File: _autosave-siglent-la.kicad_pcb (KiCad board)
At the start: 4 copper layers, 21.6 x 32.8 mm, 65 parts, among them J1 Bus_PCI_Express_x1, J10 IPEX-004, J12 IPEX-004, J13 IPEX-004, J14 IPEX-004, J15 IPEX-004, J16 IPEX-004, J17 IPEX-004, J18 IPEX-004, J19 IPEX-004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

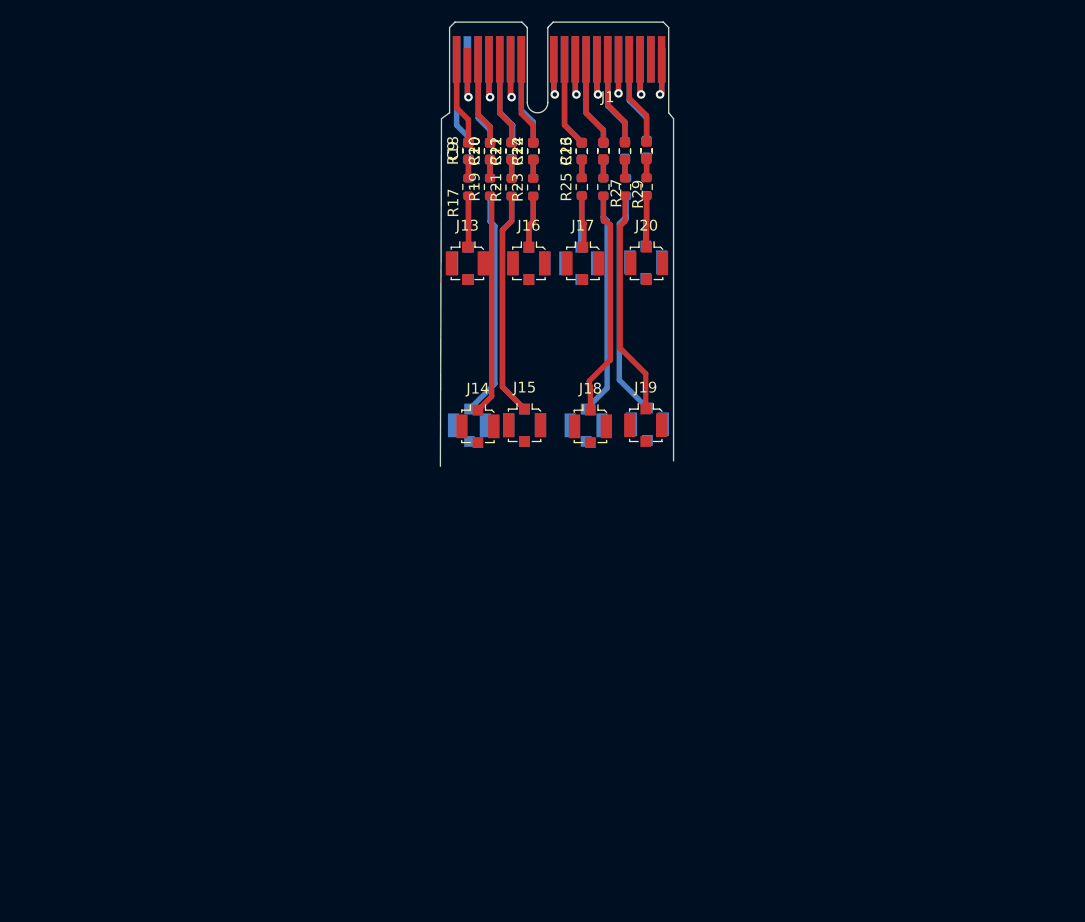
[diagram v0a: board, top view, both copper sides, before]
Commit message: rj45 version of the logic analyzer
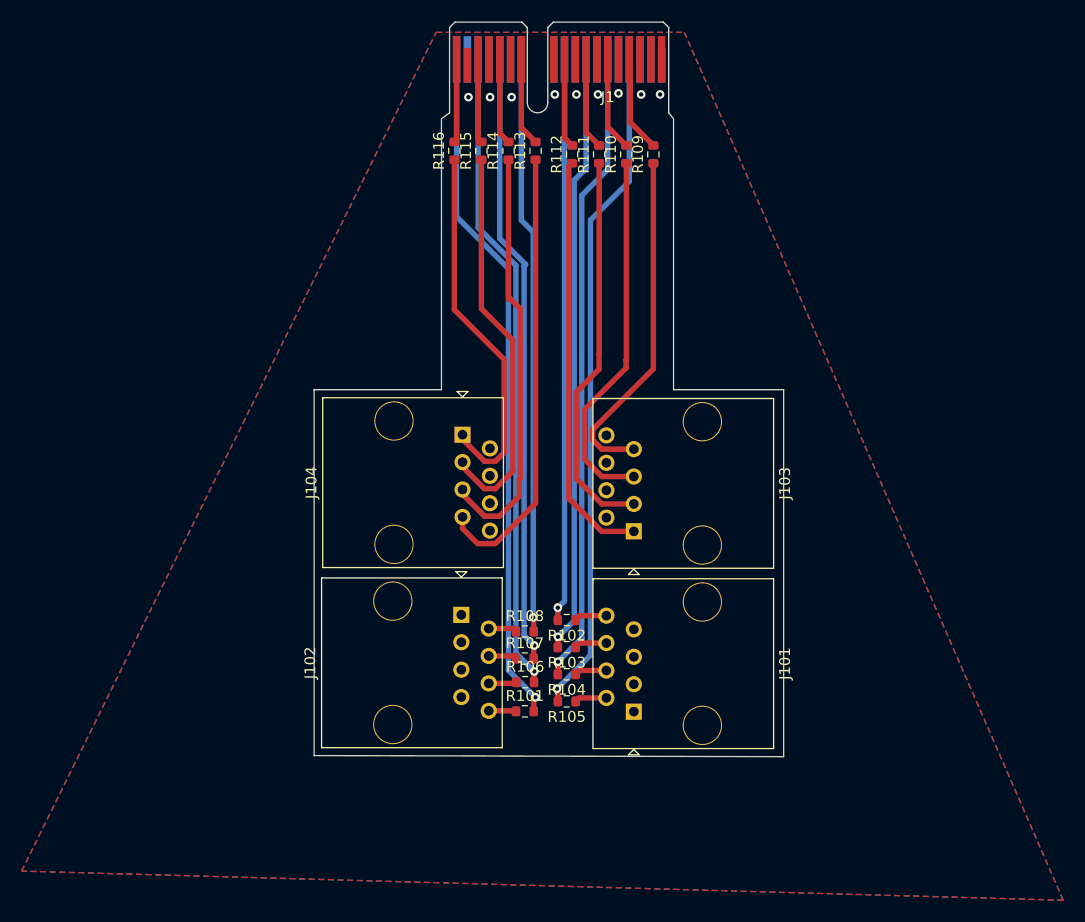
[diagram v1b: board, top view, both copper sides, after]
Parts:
- removed C1, C10, C11, C12, C13, C14, C15, C16, C2, C3, C4, C5, C6, C7, C8, C9: 8p2, Capacitor_SMD:C_0603_1608Metric
- removed J10, J12, J13, J14, J15, J16, J17, J18, J19, J2, J20, J3, J6, J7, J8, J9: IPEX-004, Connector_Coaxial:U.FL_Molex_MCRF_73412-0110_Vertical
- removed R1, R11, R13, R15, R17, R19, R21, R23, R25, R27, R29, R3, R31, R5, R7, R9: 120, Resistor_SMD:R_0603_1608Metric
- removed R10, R12, R14, R16, R18, R2, R20, R22, R24, R26, R28, R30, R32, R4, R6, R8: 91k, Resistor_SMD:R_0603_1608Metric
- added J101: RJHSE-5380, Connector_RJ:RJ45_OST_PJ012-8P8CX_Vertical, F.Cu at (117.8, 127.4)
- added J102: RJHSE-5380, Connector_RJ:RJ45_OST_PJ012-8P8CX_Vertical, F.Cu at (101.8, 118.5)
- added J103: RJHSE-5380, Connector_RJ:RJ45_OST_PJ012-8P8CX_Vertical, F.Cu at (117.8, 110.7)
- added J104: RJHSE-5380, Connector_RJ:RJ45_OST_PJ012-8P8CX_Vertical, F.Cu at (102.0, 101.8)
- added R101: 120, Resistor_SMD:R_0603_1608Metric, F.Cu at (107.7, 127.4)
- added R102: 120, Resistor_SMD:R_0603_1608Metric, F.Cu at (111.6, 118.9)
- added R103: 120, Resistor_SMD:R_0603_1608Metric, F.Cu at (111.6, 121.5)
- added R104: 120, Resistor_SMD:R_0603_1608Metric, F.Cu at (111.6, 124.0)
- added R105: 120, Resistor_SMD:R_0603_1608Metric, F.Cu at (111.6, 126.5)
- added R106: 120, Resistor_SMD:R_0603_1608Metric, F.Cu at (107.8, 124.7)
- added R107: 120, Resistor_SMD:R_0603_1608Metric, F.Cu at (107.7, 122.5)
- added R108: 120, Resistor_SMD:R_0603_1608Metric, F.Cu at (107.7, 120.0)
- added R109: 120, Resistor_SMD:R_0603_1608Metric, F.Cu at (119.6, 75.8)
- added R110: 120, Resistor_SMD:R_0603_1608Metric, F.Cu at (117.1, 75.8)
- added R111: 120, Resistor_SMD:R_0603_1608Metric, F.Cu at (114.6, 75.8)
- added R112: 120, Resistor_SMD:R_0603_1608Metric, F.Cu at (112.1, 75.8)
- added R113: 120, Resistor_SMD:R_0603_1608Metric, F.Cu at (108.7, 75.5)
- added R114: 120, Resistor_SMD:R_0603_1608Metric, F.Cu at (106.2, 75.5)
- added R115: 120, Resistor_SMD:R_0603_1608Metric, F.Cu at (103.7, 75.5)
- added R116: 120, Resistor_SMD:R_0603_1608Metric, F.Cu at (101.2, 75.5)
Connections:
- J1 pad A10: /input4/OUT -> /b.DATA_0
- J1 pad A12: /input3/OUT -> /a.DATA_3
- J1 pad A14: /input2/OUT -> /a.DATA_2
- J1 pad A16: /input1/OUT -> /a.DATA_1
- J1 pad A18: /input0/OUT -> /a.DATA_0
- J1 pad A4: /input7/OUT -> /b.DATA_3
- J1 pad A6: /input6/OUT -> /b.DATA_2
- J1 pad A8: /input5/OUT -> /b.DATA_1
- J1 pad B10: /input12/OUT -> Net-(J1-3.3Vaux)
- J1 pad B12: /input11/OUT -> Net-(J1-RSVD)
- J1 pad B14: /input10/OUT -> Net-(J1-PETp0)
- J1 pad B16: /input9/OUT -> Net-(J1-GND-PadB16)
- J1 pad B18: /input8/OUT -> Net-(J1-GND-PadB18)
- J1 pad B4: /input15/OUT -> Net-(J1-GND-PadB4)
- J1 pad B6: /input14/OUT -> Net-(J1-SMDAT)
- J1 pad B8: /input13/OUT -> Net-(J1-+3.3V-PadB8)
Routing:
- net /a.DATA_0: track 0.00 -> 63.9 mm, vias 0 -> 1
- net /b.DATA_3: track 0.00 -> 62.3 mm, vias 0 -> 1
- net /a.DATA_1: track 0.00 -> 59.9 mm, vias 0 -> 1
- net /b.DATA_2: track 0.00 -> 58.9 mm, vias 0 -> 1
- net /a.DATA_2: track 0.00 -> 57.0 mm, vias 0 -> 1
- net GND: track 56.4 -> 0.00 mm
- net /b.DATA_1: track 0.00 -> 55.5 mm, vias 0 -> 1
- net /a.DATA_3: track 0.00 -> 53.5 mm, vias 0 -> 1
- net /b.DATA_0: track 0.00 -> 52.4 mm, vias 0 -> 1
- net /d.DATA_0: track 0.00 -> 41.8 mm
- net /d.DATA_1: track 0.00 -> 39.1 mm
- net /c.DATA_3: track 0.00 -> 38.5 mm
- net /d.DATA_2: track 0.00 -> 36.7 mm
- net /c.DATA_2: track 0.00 -> 36.4 mm
- net /d.DATA_3: track 0.00 -> 34.5 mm
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- added copper zone on B.Cu, net GND
- added copper zone on F.Cu, net GND
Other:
- board size 21.6 x 32.8 mm -> 43.5 x 59.6 mm
